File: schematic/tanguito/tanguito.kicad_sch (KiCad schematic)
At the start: 14 parts, among them J1 Barrel_Jack, M1 DC Motor 12V, M2 DC Motor 12V, M3 DC Motor 12V, U2 L298N, U3 L298N

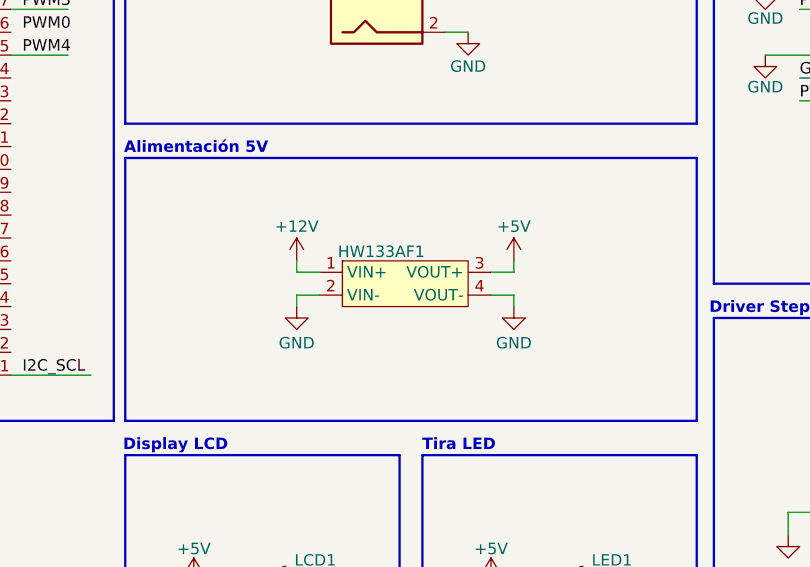
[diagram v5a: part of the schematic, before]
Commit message: update: actualizando el esquematico y la huella del stepdwon (MP1584) y faltan concluir si usar pines macho o pads con tornillos en la PCB
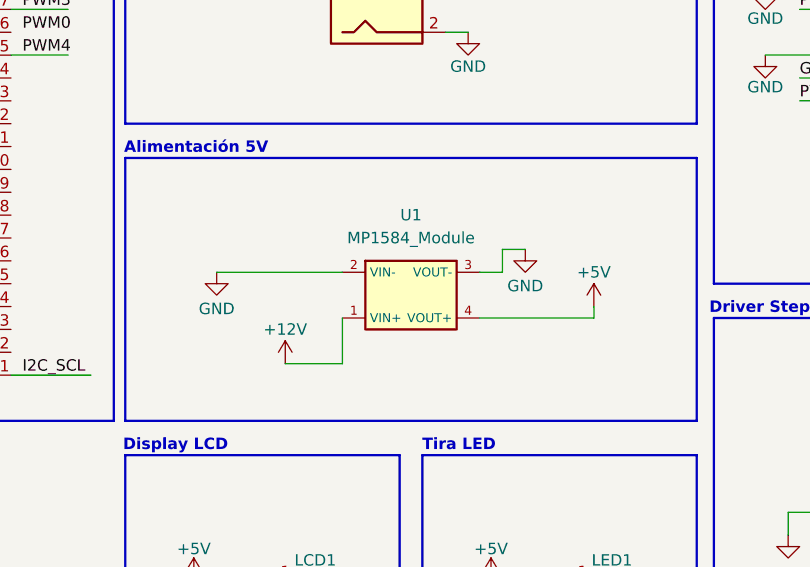
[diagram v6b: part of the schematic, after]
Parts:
- removed HW133AF1: (no value), symbol tanguito:HW133AF
- added U1: MP1584_Module, MP1584_TodoMicro:MP1584_Module_TodoMicro_22x17, symbol MP1584_Module:MP1584_Module
- MST1: footprint Connector_PinHeader_1.00mm:PinHeader_1x04_P1.00mm_Vertical -> Connector_PinHeader_2.54mm:PinHeader_1x04_P2.54mm_Vertical
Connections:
- net +12V: now also U1.1 (VIN+)
- net +5V: now also U1.4 (VOUT+)
- net GND: now also U1.2 (VIN-), U1.3 (VOUT-)
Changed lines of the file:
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@@
 	(wire
 		(pts
-			(xy 154.94 62.23) (xy 152.4 62.23)
-		)
-		(stroke
-			(width 0)
-			(type default)
-		)
-	)
-	(wire
-		(pts
 			(xy 57.15 50.8) (xy 50.8 50.8)
 		)
@@
 	(wire
 		(pts
-			(xy 154.94 59.69) (xy 152.4 59.69)
-		)
-		(stroke
-			(width 0)
-			(type default)
-		)
-	)
-	(wire
-		(pts
 			(xy 228.6 40.64) (xy 223.52 40.64)
 		)
@@
 	(wire
 		(pts
-			(xy 186.69 40.64) (xy 193.04 40.64)
+			(xy 129.54 69.85) (xy 135.89 69.85)
 		)
 		(stroke
@@
 	(wire
 		(pts
-			(xy 154.94 62.23) (xy 154.94 63.5)
+			(xy 186.69 40.64) (xy 193.04 40.64)
 		)
 		(stroke
@@
 	(wire
 		(pts
-			(xy 130.81 58.42) (xy 130.81 59.69)
+			(xy 153.67 57.15) (xy 156.21 57.15)
 		)
 		(stroke
@@
 	(wire
 		(pts
-			(xy 130.81 62.23) (xy 133.35 62.23)
+			(xy 121.92 59.69) (xy 135.89 59.69)
 		)
 		(stroke
@@
 	(wire
 		(pts
-			(xy 154.94 58.42) (xy 154.94 59.69)
+			(xy 163.83 63.5) (xy 163.83 64.77)
 		)
 		(stroke
@@
 	(wire
 		(pts
+			(xy 135.89 69.85) (xy 135.89 64.77)
+		)
+		(stroke
+			(width 0)
+			(type default)
+		)
+	)
+	(wire
+		(pts
 			(xy 218.44 86.36) (xy 224.79 86.36)
 		)
@@
 	(wire
 		(pts
+			(xy 151.13 59.69) (xy 153.67 59.69)
+		)
+		(stroke
+			(width 0)
+			(type default)
+		)
+	)
+	(wire
+		(pts
 			(xy 50.8 40.64) (xy 57.15 40.64)
 		)
@@
 	(wire
 		(pts
-			(xy 130.81 59.69) (xy 133.35 59.69)
+			(xy 151.13 64.77) (xy 163.83 64.77)
 		)
 		(stroke
@@
 	(wire
 		(pts
-			(xy 119.38 96.52) (xy 128.27 96.52)
+			(xy 153.67 59.69) (xy 153.67 57.15)
 		)
 		(stroke
@@
 	(wire
 		(pts
-			(xy 130.81 63.5) (xy 130.81 62.23)
+			(xy 119.38 96.52) (xy 128.27 96.52)
 		)
 		(stroke
@@
 	(symbol
 		(lib_id "power:+5V")
-		(at 154.94 58.42 0)
+		(at 163.83 63.5 0)
 		(unit 1)
 		(body_style 1)
@@
 		(dnp no)
 		(property "Reference" "#PWR011"
-			(at 154.94 62.23 0)
+			(at 163.83 67.31 0)
 			(hide yes)
 			(show_name no)
@@
 		)
 		(property "Value" "+5V"
-			(at 154.94 54.61 0)
+			(at 163.83 59.69 0)
 			(show_name no)
 			(do_not_autoplace no)
@@
 		)
 		(property "Footprint" ""
-			(at 154.94 58.42 0)
+			(at 163.83 63.5 0)
 			(hide yes)
 			(show_name no)
@@
 		)
 		(property "Datasheet" ""
-			(at 154.94 58.42 0)
+			(at 163.83 63.5 0)
 			(hide yes)
 			(show_name no)
@@
 		)
 		(property "Description" "Power symbol creates a global label with name \"+5V\""
-			(at 154.94 58.42 0)
+			(at 163.83 63.5 0)
 			(hide yes)
 			(show_name no)
@@
 	(symbol
 		(lib_id "power:GND")
-		(at 130.81 63.5 0)
+		(at 121.92 59.69 0)
 		(unit 1)
 		(body_style 1)
@@
 		(dnp no)
 		(property "Reference" "#PWR06"
-			(at 130.81 69.85 0)
+			(at 121.92 66.04 0)
 			(hide yes)
 			(show_name no)
@@
 		)
 		(property "Value" "GND"
-			(at 130.81 67.564 0)
+			(at 121.92 63.754 0)
 			(show_name no)
 			(do_not_autoplace no)
@@
 		)
 		(property "Footprint" ""
-			(at 130.81 63.5 0)
+			(at 121.92 59.69 0)
 			(hide yes)
 			(show_name no)
@@
 		)
 		(property "Datasheet" ""
-			(at 130.81 63.5 0)
+			(at 121.92 59.69 0)
 			(hide yes)
 			(show_name no)
@@
 		)
 		(property "Description" "Power symbol creates a global label with name \"GND\" , ground"
-			(at 130.81 63.5 0)
+			(at 121.92 59.69 0)
 			(hide yes)
 			(show_name no)
@@
 	(symbol
 		(lib_id "power:+12V")
-		(at 130.81 58.42 0)
+		(at 129.54 69.85 0)
 		(unit 1)
 		(body_style 1)
@@
 		(dnp no)
 		(property "Reference" "#PWR05"
-			(at 130.81 62.23 0)
+			(at 129.54 73.66 0)
 			(hide yes)
 			(show_name no)
@@
 		)
 		(property "Value" "+12V"
-			(at 130.81 54.61 0)
+			(at 129.54 66.04 0)
 			(show_name no)
 			(do_not_autoplace no)
@@
 		)
 		(property "Footprint" ""
-			(at 130.81 58.42 0)
+			(at 129.54 69.85 0)
 			(hide yes)
 			(show_name no)
@@
 		)
 		(property "Datasheet" ""
-			(at 130.81 58.42 0)
+			(at 129.54 69.85 0)
 			(hide yes)
 			(show_name no)
@@
 		)
 		(property "Description" "Power symbol creates a global label with name \"+12V\""
-			(at 130.81 58.42 0)
+			(at 129.54 69.85 0)
 			(hide yes)
 			(show_name no)
@@
 	(symbol
 		(lib_id "power:GND")
-		(at 154.94 63.5 0)
+		(at 156.21 57.15 0)
 		(unit 1)
 		(body_style 1)
@@
 		(dnp no)
 		(property "Reference" "#PWR012"
-			(at 154.94 69.85 0)
+			(at 156.21 63.5 0)
 			(hide yes)
 			(show_name no)
@@
 		)
 		(property "Value" "GND"
-			(at 154.94 67.564 0)
+			(at 156.21 61.214 0)
 			(show_name no)
 			(do_not_autoplace no)
@@
 		)
 		(property "Footprint" ""
-			(at 154.94 63.5 0)
+			(at 156.21 57.15 0)
 			(hide yes)
 			(show_name no)
@@
 		)
 		(property "Datasheet" ""
-			(at 154.94 63.5 0)
+			(at 156.21 57.15 0)
 			(hide yes)
 			(show_name no)
@@
 		)
 		(property "Description" "Power symbol creates a global label with name \"GND\" , ground"
-			(at 154.94 63.5 0)
+			(at 156.21 57.15 0)
 			(hide yes)
 			(show_name no)
@@
 	)
 	(symbol
+		(lib_id "MP1584_Module:MP1584_Module")
+		(at 143.51 62.23 0)
+		(unit 1)
+		(body_style 1)
+		(exclude_from_sim no)
+		(in_bom yes)
+		(on_board yes)
+		(in_pos_files yes)
+		(dnp no)
+		(fields_autoplaced yes)
+		(property "Reference" "U1"
+			(at 143.51 53.34 0)
+			(show_name no)
+			(do_not_autoplace no)
+			(effects
+				(font
+					(size 1.27 1.27)
+				)
+			)
+		)
+		(property "Value" "MP1584_Module"
+			(at 143.51 55.88 0)
+			(show_name no)
+			(do_not_autoplace no)
+			(effects
+				(font
+					(size 1.27 1.27)
+				)
+			)
+		)
+		(property "Footprint" "MP1584_TodoMicro:MP1584_Module_TodoMicro_22x17"
+			(at 143.51 62.23 0)
+			(hide yes)
+			(show_name no)
+			(do_not_autoplace no)
+			(effects
+				(font
+					(size 1.27 1.27)
+				)
+			)
+		)
+		(property "Datasheet" "https://www.todomicro.com.ar/616-regulador-step-down-mp1584-salida-15-a-26v-3a.html"
+			(at 143.51 62.23 0)
+			(hide yes)
+			(show_name no)
+			(do_not_autoplace no)
+			(effects
+				(font
+					(size 1.27 1.27)
+				)
+			)
+		)
+		(property "Description" ""
+			(at 143.51 62.23 0)
+			(hide yes)
+			(show_name no)
+			(do_not_autoplace no)
+			(effects
+				(font
+					(size 1.27 1.27)
+				)
+			)
+		)
+		(pin "1"
+		)
+		(pin "4"
+		)
+		(pin "2"
+		)
+		(pin "3"
+		)
+		(instances
+			(project "tanguito"
+				(path "/9a9dbedc-f647-45f6-bf2f-0ae89a9fba5f"
+					(reference "U1")
+					(unit 1)
+				)
+			)
+		)
+	)
+	(symbol
 		(lib_id "Motor:Stepper_Motor_bipolar")
 		(at 257.81 92.71 0)
@@
 			)
 		)
-		(property "Footprint" "Connector_PinHeader_1.00mm:PinHeader_1x04_P1.00mm_Vertical"
+		(property "Footprint" "Connector_PinHeader_2.54mm:PinHeader_1x04_P2.54mm_Vertical"
 			(at 258.064 92.964 0)
 			(hide yes)
@@
 					(unit 1)
 				)
-			)
-		)
-	)
-	(symbol
-		(lib_id "tanguito:HW133AF")
-		(at 140.97 55.88 0)
-		(unit 1)
-		(body_style 1)
-		(exclude_from_sim no)
-		(in_bom yes)
-		(on_board yes)
-		(in_pos_files yes)
-		(dnp no)
-		(property "Reference" "HW133AF1"
-			(at 140.208 57.404 0)
-			(show_name no)
-			(do_not_autoplace no)
-			(effects
-				(font
-					(size 1.27 1.27)
-				)
-			)
-		)
-		(property "Value" ""
-			(at 140.97 55.88 0)
-			(show_name no)
-			(do_not_autoplace no)
-			(effects
-				(font
-					(size 1.27 1.27)
-				)
-			)
-		)
-		(property "Footprint" ""
-			(at 140.97 55.88 0)
-			(hide yes)
-			(show_name no)
-			(do_not_autoplace no)
-			(effects
-				(font
-					(size 1.27 1.27)
-				)
-			)
-		)
-		(property "Datasheet" ""
-			(at 140.97 55.88 0)
-			(hide yes)
-			(show_name no)
-			(do_not_autoplace no)
-			(effects
-				(font
-					(size 1.27 1.27)
-				)
-			)
-		)
-		(property "Description" ""
-			(at 140.97 55.88 0)
-			(hide yes)
-			(show_name no)
-			(do_not_autoplace no)
-			(effects
-				(font
-					(size 1.27 1.27)
-				)
-			)
-		)
-		(pin "2"
-		)
-		(pin "4"
-		)
-		(pin "1"
-		)
-		(pin "3"
-		)
-		(instances
-			(project "tanguito"
-				(path "/9a9dbedc-f647-45f6-bf2f-0ae89a9fba5f"
-					(reference "HW133AF1")
-					(unit 1)
-				)

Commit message: update: se cambiaron las huellas en el esquematico del LCD y del LED para que sean pads de 1x4 con pin patch de 2.54mm y se confirmo que el stepper ya cuenta con esa huella
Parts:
- LCD1, LED1: footprint Connector_PinHeader_1.00mm:PinHeader_1x04_P1.00mm_Vertical -> Connector_PinHeader_2.54mm:PinHeader_1x04_P2.54mm_Vertical
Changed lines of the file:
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@@
 			)
 		)
-		(property "Footprint" "Connector_PinHeader_1.00mm:PinHeader_1x04_P1.00mm_Vertical"
+		(property "Footprint" "Connector_PinHeader_2.54mm:PinHeader_1x04_P2.54mm_Vertical"
 			(at 166.37 91.44 0)
 			(hide yes)
@@
 			)
 		)
-		(property "Footprint" "Connector_PinHeader_1.00mm:PinHeader_1x04_P1.00mm_Vertical"
+		(property "Footprint" "Connector_PinHeader_2.54mm:PinHeader_1x04_P2.54mm_Vertical"
 			(at 135.89 90.17 0)
 			(hide yes)

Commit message: diseño electrico y de PCB actualizados, pero faltan las pistas
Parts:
- J1: footprint TerminalBlock:TerminalBlock_MaiXu_MX126-5.0-02P_1x02_P5.00mm -> Connector_PinHeader_2.54mm:PinHeader_1x02_P2.54mm_Vertical
- U2: footprint Package_TO_SOT_THT:TO-220-15_P2.54x5.08mm_StaggerOdd_Lead4.58mm_Vertical -> Connector_PinHeader_2.54mm:PinHeader_1x10_P2.54mm_Vertical
- U3: footprint Package_TO_SOT_THT:TO-220-15_P2.54x5.08mm_StaggerOdd_Lead4.58mm_Vertical -> Connector_PinHeader_2.54mm:PinHeader_1x07_P2.54mm_Vertical
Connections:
- net +12V: now also U2.6 (Vs); no longer U2.4 (Vs)
- net GND: now also U2.1 (GND), U3.1 (GND); no longer U2.7 (IN2), U3.8 (GND)
- net GPIO0: now also U2.7 (IN1); no longer U2.5 (IN1)
- net M1+: now also U2.5 (OUT1); no longer U2.2 (OUT1)
- net M1-: now also U2.4 (OUT2); no longer U2.3 (OUT2)
- net M2+: now also U2.3 (OUT3); no longer U2.13 (OUT3)
- net M2-: now also U2.2 (OUT4); no longer U2.14 (OUT4)
- net PWM0: now also P1.36 (T_FL1), U2.9 (EnA); no longer U2.6 (EnA)
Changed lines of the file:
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@@
 	(wire
 		(pts
+			(xy 99.06 33.02) (xy 100.33 33.02)
+		)
+		(stroke
+			(width 0)
+			(type default)
+		)
+	)
+	(wire
+		(pts
 			(xy 153.67 59.69) (xy 153.67 57.15)
 		)
@@
 			)
 		)
-		(property "Footprint" "Package_TO_SOT_THT:TO-220-15_P2.54x5.08mm_StaggerOdd_Lead4.58mm_Vertical"
+		(property "Footprint" "Connector_PinHeader_2.54mm:PinHeader_1x07_P2.54mm_Vertical"
 			(at 209.55 158.75 0)
 			(hide yes)
@@
 			)
 		)
-		(property "Footprint" "TerminalBlock:TerminalBlock_MaiXu_MX126-5.0-02P_1x02_P5.00mm"
+		(property "Footprint" "Connector_PinHeader_2.54mm:PinHeader_1x02_P2.54mm_Vertical"
 			(at 140.97 31.496 0)
 			(hide yes)
@@
 	)
 	(symbol
+		(lib_name "L298N_1")
 		(lib_id "Driver_Motor:L298N")
 		(at 208.28 38.1 0)
@@
 			)
 		)
-		(property "Footprint" "Package_TO_SOT_THT:TO-220-15_P2.54x5.08mm_StaggerOdd_Lead4.58mm_Vertical"
+		(property "Footprint" "Connector_PinHeader_2.54mm:PinHeader_1x10_P2.54mm_Vertical"
 			(at 209.55 54.61 0)
 			(hide yes)
